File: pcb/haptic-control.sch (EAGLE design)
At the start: 146 parts, among them M1 SPH0641LM4H-1, P1 2P-PAD_1X3.5, P2 2P-PAD_1X3.5, P3 2P-PAD_1X3.5, P4 2P-PAD_1X3.5, U1 MIC23159, U10 DRV2605L, U11 DRV2605L, U12 MTCH6301, U2 BQ51050B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

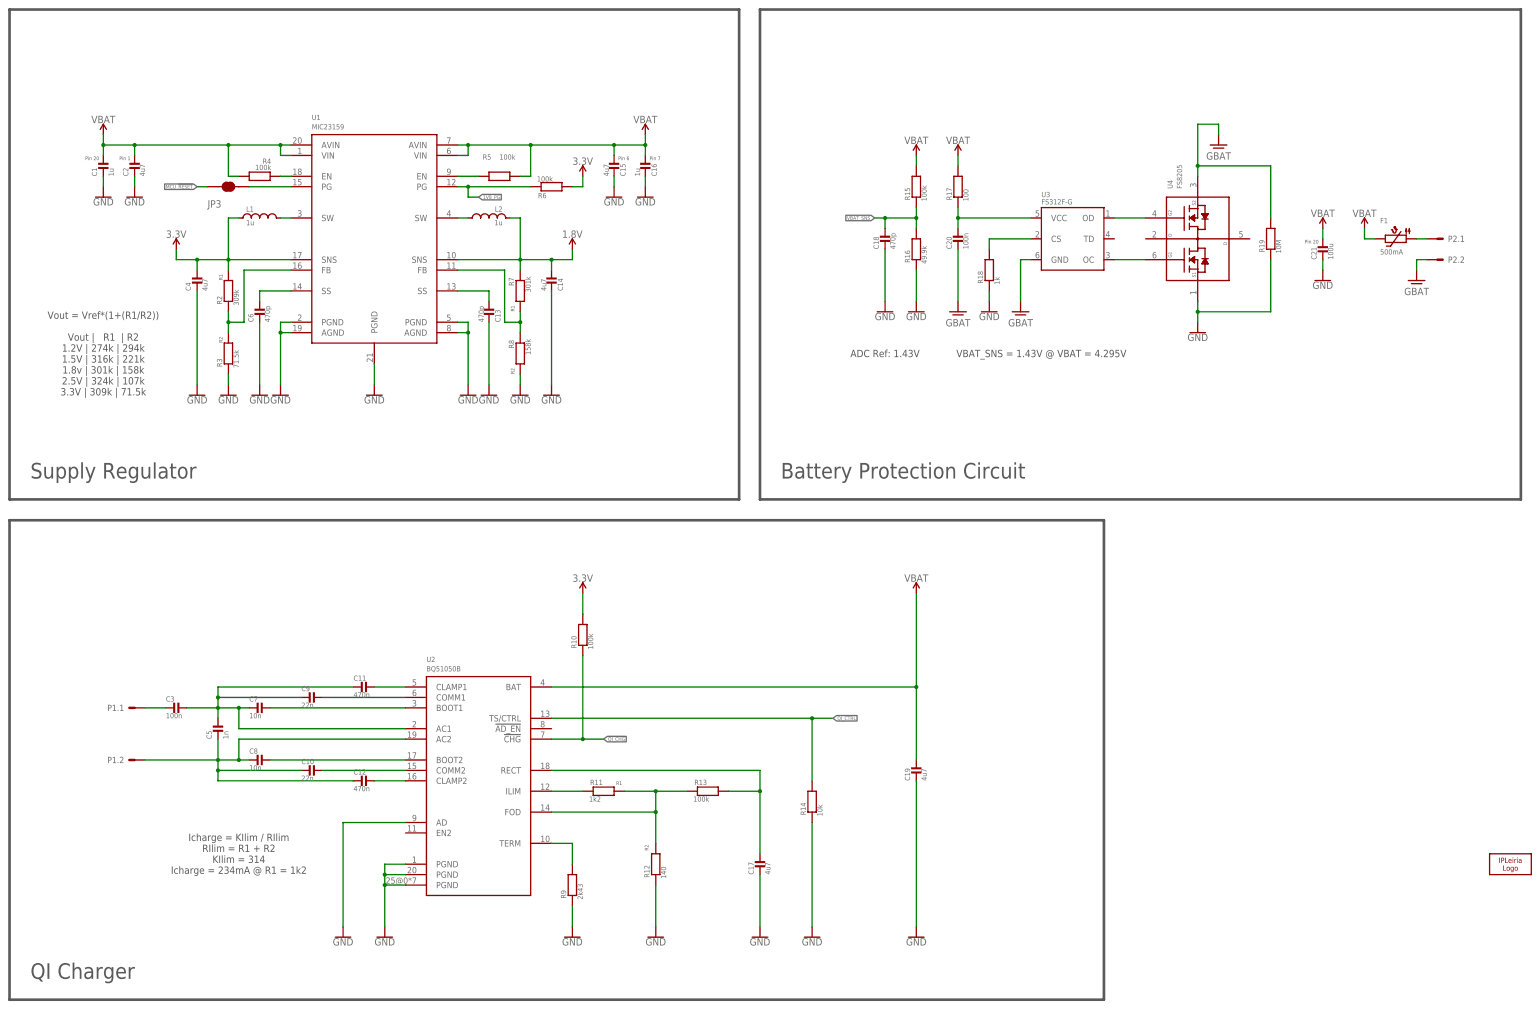
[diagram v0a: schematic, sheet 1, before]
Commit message: changed component values, created bom, changed bat prot ic
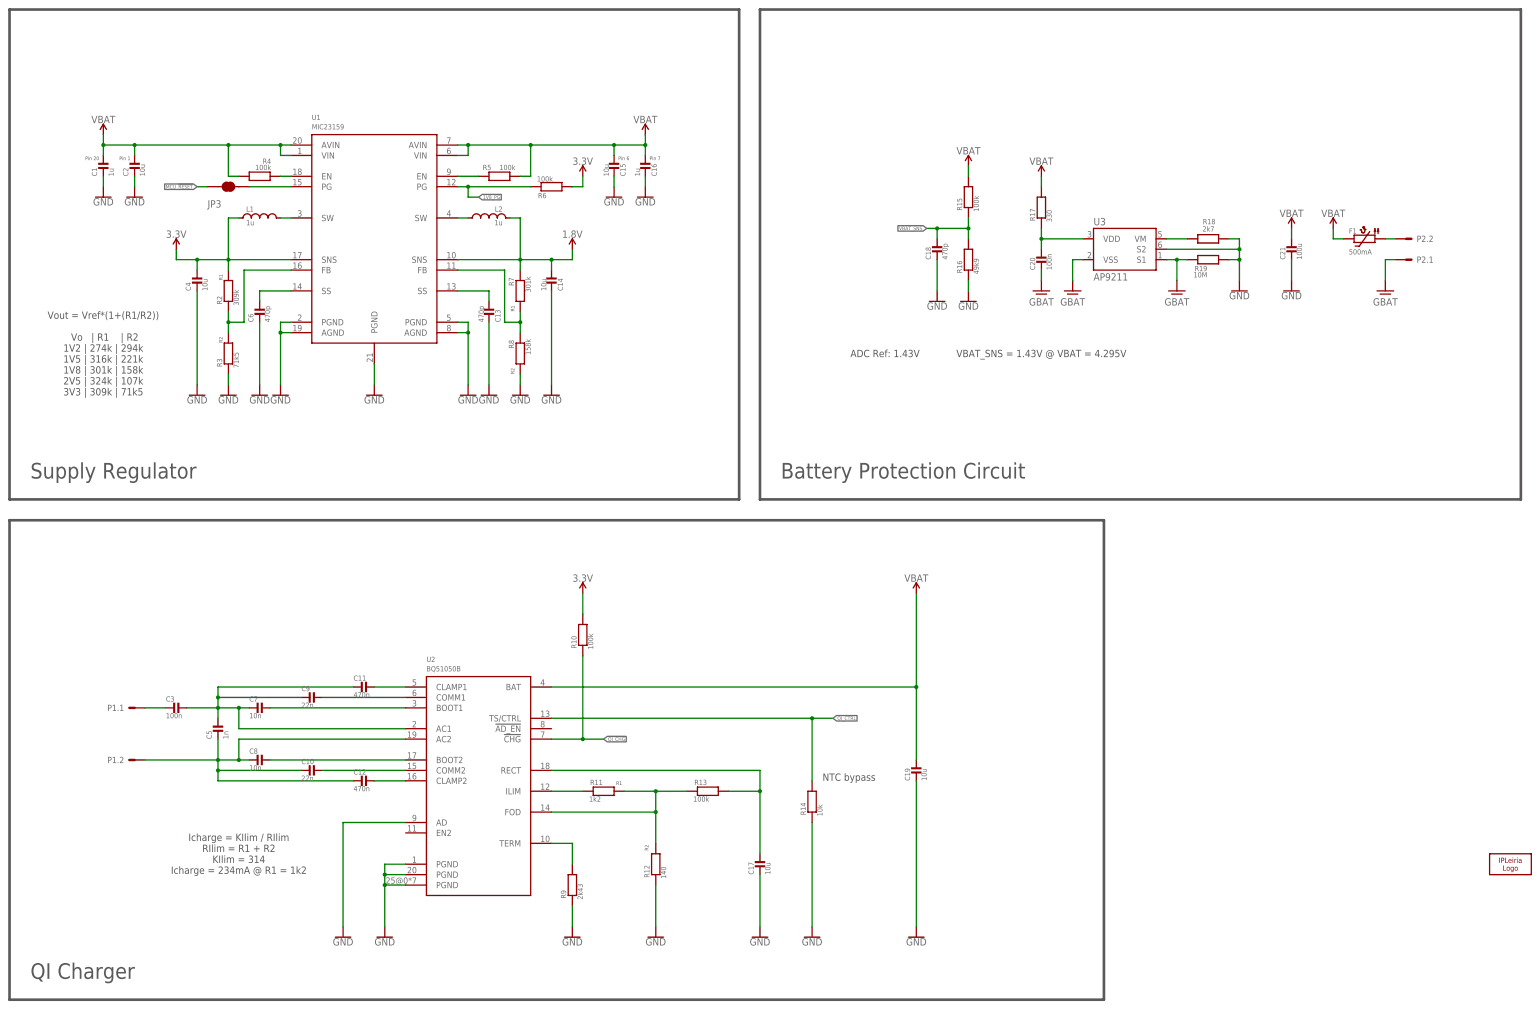
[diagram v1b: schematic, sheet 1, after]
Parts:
- removed U4: FS8205, Fortune:FS8205
- added R1, R38: 100k, Passive Components > Resistors > Chip Resistors:RESISTOR_0402
- added SCL, SDA: TEST_POINT, Utility > Board:TEST_POINT
- C14, C15, C17, C19, C2, C4: value 4u7 -> 10u
- L4, L5: value 2N -> 2n
- R16: value 49.9k -> 49k9
- R17: value 100 -> 330
- R18: value 1k -> 2k7
- R3: value 71.5k -> 71k5
- R30, R32, R34, R36: value 3.4k -> 3k4
- U3: value FS312F-G -> AP9211; device Fortune:FS312F-G -> Power > Battery Management:AP9211
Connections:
- removed net LRA_EN: U10.EN, U11.EN, U5.DIO_8
- removed net N$24: R18.P$2, U3.CS
- removed net N$38: F1.1, P2.1.S
- removed net PCAP_RX10: U12.RX10
- removed net PCAP_RX11: U12.RX11
- removed net PCAP_RX12: U12.RX12
- removed net PCAP_RX9: U12.RX9
- removed net PCAP_TX10: U12.TX10
- removed net PCAP_TX11: U12.TX11
- removed net PCAP_TX12: U12.TX12
- removed net PCAP_TX13: U12.TX13
- removed net PCAP_TX14: U12.TX14
- removed net PCAP_TX15: U12.TX15
- removed net PCAP_TX16: U12.TX16
- removed net PCAP_TX17: U12.TX17
- removed net PCAP_TX4: U12.TX4
- removed net PCAP_TX5: U12.TX5
- removed net PCAP_TX6: U12.TX6
- removed net PCAP_TX7: U12.TX7
- removed net PCAP_TX8: U12.TX8
- removed net PCAP_TX9: U12.TX9
- new net LRA1_EN: R1.P$1, U10.EN, U5.DIO_8
- new net LRA2_EN: R38.P$1, U11.EN, U5.DIO_11
- net 3.3V: now also R1.P$2, R38.P$2
- net GBAT: now also P2.1.S, R19.P$1, U3.S1@1, U3.VSS@2; no longer P2.2.S, R19.P$2, U3.GND, U4.S2
- net GND: now also R19.P$2, U3.S2@6; no longer R19.P$1, U4.S1
- net N$21: now also R18.P$2, U3.VM@5; no longer U3.OD, U4.G2
- net N$22: now also F1.1, P2.2.S; no longer U3.OC, U4.G1
- net N$23: now also U3.VDD@3; no longer U3.VCC
- net SCL: now also SCL.S
- net SDA: now also SDA.S
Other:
- note added: "I2C Address: 0x5A"
- note added: "I2C Bradcast Address: 0x58"
- note added: "NTC bypass"
- note added: "Vout = Vref*(1+(R1/R2)) Vo | R1 | R2 1V2 | 274k | 294k 1V5 | 316k | 221k 1V8 | 301k | 158k 2V5 | 324k | 107k 3V3 | 309k | 71k5"
- note removed: "TODO: Verify Unpowered VREF1 Behaviour"
- note removed: "Vout = Vref*(1+(R1/R2)) Vout | R1 | R2 1.2V | 274k | 294k 1.5V | 316k | 221k 1.8v | 301k | 158k 2.5V | 324k | 107k 3.3V | 309k | 71.5k"
- moved on the sheet: C18, C20, C21, C49, F1, P2.1, P2.2, R15, R16, R17, R18, R19
